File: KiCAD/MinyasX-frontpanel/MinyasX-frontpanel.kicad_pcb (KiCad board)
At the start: 2 copper layers, 96 x 21 mm, 30 parts, among them J101 Conn_01x04, J102 Conn_02x06_Odd_Even, SW101 SW_Push, SW102 SW_Push, U101 SLG46826G(V2), U102 JOYSTICK, U17 XC6201P332MR-G, U22 PCA9515DP

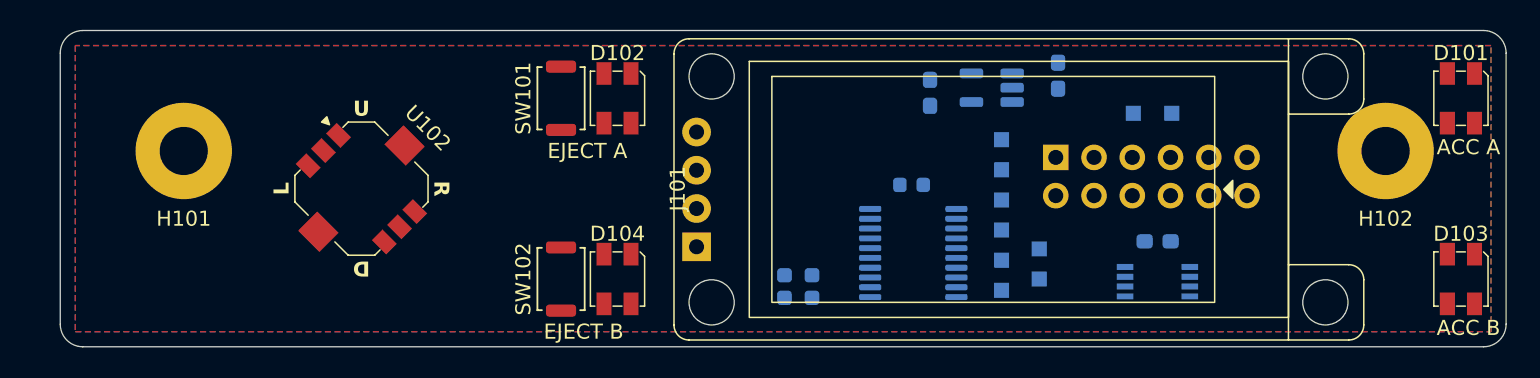
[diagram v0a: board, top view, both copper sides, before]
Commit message: * フロントパネルのキー操作ができるようにした * 画面のページ切り替えができるようにした * FDDの回転数とbpsの推定コードを修正した
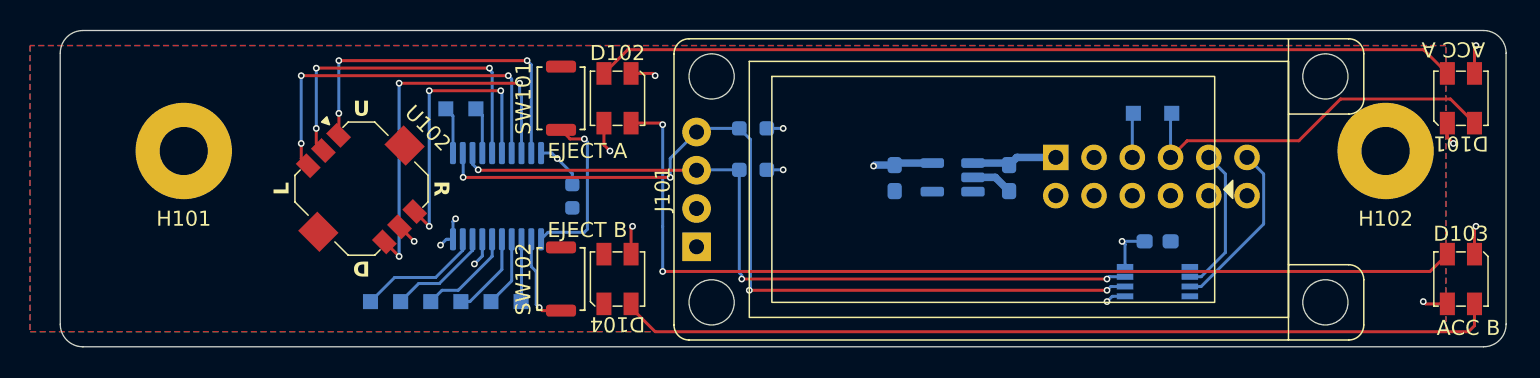
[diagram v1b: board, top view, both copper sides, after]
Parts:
- moved TP105 42.5 mm to (124.6, 95.0)
- moved TP106 42.0 mm to (122.6, 95.0)
- moved TP107 39.1 mm to (129.6, 82.2)
- moved TP108 38.8 mm to (127.6, 82.2)
- moved TP104 38.2 mm to (126.6, 95.0)
- moved TP103 36.5 mm to (128.6, 95.0)
- moved TP102 35.0 mm to (130.6, 95.0)
- moved TP101 33.7 mm to (132.6, 95.0)
- moved U101 27.9 mm to (131.0, 88.0), turned to 90 degrees
- moved C101 22.5 mm to (136.0, 88.0), turned to -90 degrees
- moved R31 11.6 mm to (148.0, 83.5), turned to 180 degrees
- moved R30 7.62 mm to (148.0, 86.2), turned to 180 degrees
- moved C25 7.54 mm to (165.0, 86.8)
- moved U17 6.49 mm to (161.2, 86.8)
- moved C26 6.13 mm to (157.4, 86.8)
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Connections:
- TP101 pad 1: Net-(U101-IO14) -> Net-(U101-IO12)
- TP102 pad 1: Net-(U101-IO13) -> Net-(U101-IO11)
- TP103 pad 1: Net-(U101-IO12) -> Net-(U101-IO10)
- TP104 pad 1: Net-(U101-IO11) -> Net-(U101-IO9)
- TP105 pad 1: Net-(U101-IO10) -> Net-(U101-IO8)
- TP106 pad 1: Net-(U101-IO9) -> Net-(U101-IO7)
- TP107 pad 1: Net-(U101-IO8) -> Net-(U101-IO5)
- TP108 pad 1: Net-(U101-IO7) -> Net-(U101-IO6)
- U101 pad 1: Net-(U101-IO14) -> /EJECT_A
- U101 pad 11: /EJECT_B -> Net-(U101-IO6)
- U101 pad 14: /EJECT_A -> Net-(U101-IO5)
- U101 pad 2: Net-(U101-IO13) -> /EJECT_B
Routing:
- net Net-(D102-DOUT): track 0.00 -> 64.5 mm, vias 0 -> 2
- net Net-(D103-DOUT): track 0.00 -> 58.5 mm
- net /I2C_SDA: track 0.00 -> 58.2 mm, vias 0 -> 4
- net Net-(D101-DOUT): track 0.00 -> 57.3 mm
- net /I2C_SCL: track 0.00 -> 51.5 mm, vias 0 -> 3
- net /DOWN: track 0.00 -> 25.6 mm, vias 0 -> 3
- net /LED_DATA: track 0.00 -> 25.4 mm
- net /LEFT: track 0.00 -> 25.2 mm, vias 0 -> 3
- net /UP: track 0.00 -> 23.7 mm, vias 0 -> 3
- net /CENTER: track 0.00 -> 23.0 mm, vias 0 -> 3
- net /RIGHT: track 0.00 -> 19.3 mm, vias 0 -> 3
- net +3.3V: track 0.00 -> 16.2 mm, vias 0 -> 7
- net VDD_MCU: track 0.00 -> 13.2 mm, vias 0 -> 4
- net GND: track 0.00 -> 11.7 mm, vias 0 -> 6
- net /I2C_SDA_5V: track 0.00 -> 11.5 mm
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- added copper zone on In1.Cu, net +3.3V
- added copper zone on In2.Cu, net VDD_MCU
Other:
- copper layers 2 -> 4

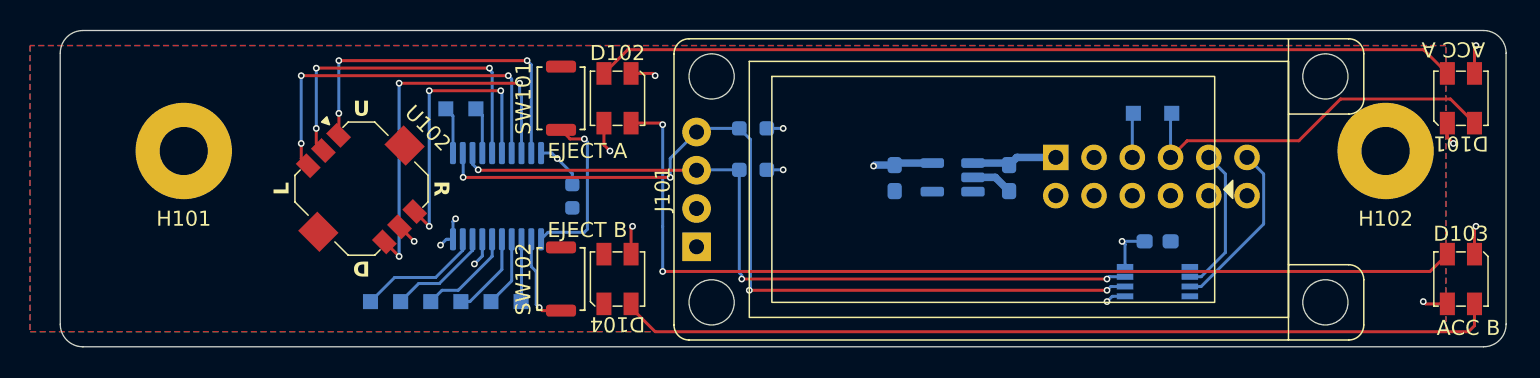
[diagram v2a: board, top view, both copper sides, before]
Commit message: フロントパネル周りの配線を見直した
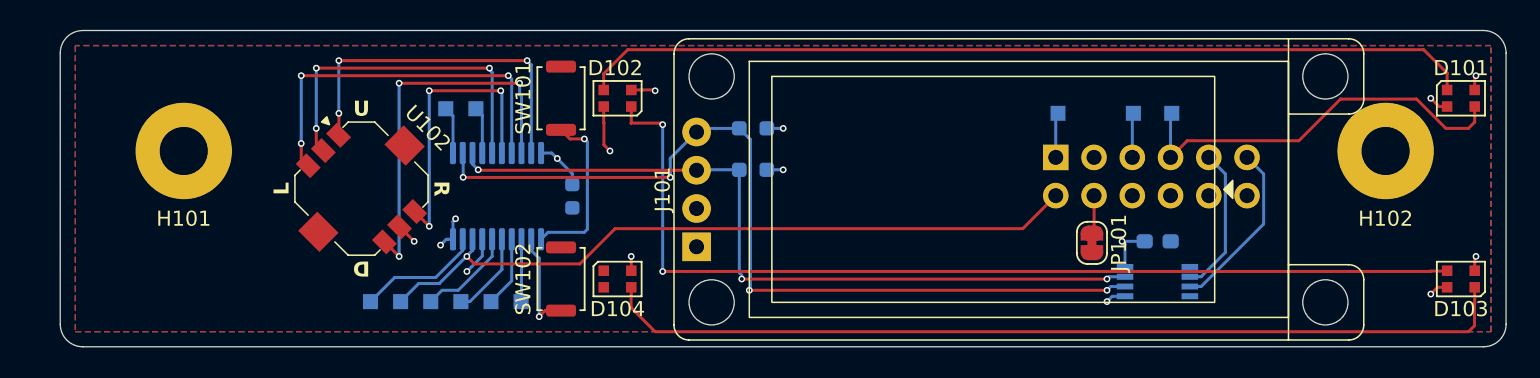
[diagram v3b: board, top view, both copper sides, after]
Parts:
- removed C25, C26: 1uF, Capacitor_SMD:C_0603_1608Metric_Pad1.08x0.95mm_HandSolder
- removed U17: XC6201P332MR-G, Package_TO_SOT_SMD:SOT-23-5_HandSoldering
- added JP101: Jumper_2_Bridged, Jumper:SolderJumper-2_P1.3mm_Bridged_RoundedPad1.0x1.5mm, F.Cu at (170.5, 91.1)
- added TP110: TestPoint, TestPoint:TestPoint_Pad_1.0x1.0mm, B.Cu at (173.2, 82.5)
- D101, D102, D103, D104: value SK6812MINI -> WS2812B-2020; footprint x68k-lib:SK6812MINI-HS -> LED_SMD:LED_WS2812B-2020_PLCC4_2.0x2.0mm
- moved TP109 5.00 mm to (168.2, 82.5)
- turned D101 to 0 degrees
- turned D102 to 180 degrees
- turned D103 to 180 degrees
- turned D104 to 0 degrees
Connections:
- D101 pad 1: GND -> Net-(D101-DOUT)
- D101 pad 2: /LED_DATA -> GND
- D101 pad 3: VDD_MCU -> /LED_DATA
- D101 pad 4: Net-(D101-DOUT) -> VDD_MCU
- D102 pad 1: GND -> Net-(D102-DOUT)
- D102 pad 2: Net-(D101-DOUT) -> GND
- D102 pad 3: VDD_MCU -> Net-(D101-DOUT)
- D102 pad 4: Net-(D102-DOUT) -> VDD_MCU
- D103 pad 1: GND -> Net-(D103-DOUT)
- D103 pad 2: Net-(D102-DOUT) -> GND
- D103 pad 3: VDD_MCU -> Net-(D102-DOUT)
- D103 pad 4: Net-(D103-DOUT) -> VDD_MCU
- D104 pad 1: GND -> unconnected-(D104-DOUT-Pad1)
- D104 pad 2: Net-(D103-DOUT) -> GND
- D104 pad 3: VDD_MCU -> Net-(D103-DOUT)
- D104 pad 4: unconnected-(D104-DOUT-Pad4) -> VDD_MCU
- J102 pad 2: GND -> /CONT_PUSH
- J102 pad 4: GND -> Net-(J102-Pin_4)
- J102 pad 5: /CONTROLLER_OPTION -> +3.3V
- TP105 pad 1: Net-(U101-IO8) -> /CONT_PUSH
- TP109 pad 1: /CONTROLLER_OPTION -> VDD_MCU
- U101 pad 8: Net-(U101-IO8) -> /CONT_PUSH
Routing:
- net /CONT_PUSH: track 0.00 -> 48.1 mm, vias 0 -> 1
- net Net-(U101-IO8): track 6.92 -> 0.00 mm
- net GND: track 11.7 -> 7.70 mm
- net VDD_MCU: track 13.2 -> 9.32 mm
- net /CONTROLLER_OPTION: track 2.95 -> 0.00 mm
- net Net-(J102-Pin_4): track 0.00 -> 2.54 mm
- net Net-(D103-DOUT): track 58.5 -> 60.7 mm
- net Net-(D101-DOUT): track 57.3 -> 59.5 mm
- net /LED_DATA: track 25.4 -> 26.8 mm
- net /EJECT_B: track 6.29 -> 6.97 mm
- net Net-(D102-DOUT): track 64.5 -> 65.1 mm
- net +3.3V: track 16.2 -> 15.7 mm, vias 7 -> 6
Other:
- board text added: "3.3"
- board text added: "LED"
- board text added: "VDD"

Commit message: v2.1.0のPCBA発注
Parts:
- renumbered C101 to C2001, C37 to C2002, D101 to D2001, D102 to D2002, D103 to D2003, D104 to D2004, H101 to H2001, H102 to H2002, J102 to J2001, J101 to J2002, JP101 to JP2001, R30 to R2001, R31 to R2002, SW101 to SW2001, SW102 to SW2002, TP109 to TP2001, TP110 to TP2002, TP112 to TP2003, TP101 to TP2004, TP102 to TP2005, TP103 to TP2006, TP104 to TP2007, TP105 to TP2008, TP106 to TP2009, TP107 to TP2010, TP108 to TP2011, U101 to U2001, U22 to U2002, U102 to U2003

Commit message: 細かい基板のパッチを当てた * MODE_SELECT をGPからドライブできるように配線した * FDD電源出力コネクタを少し外に出した * GP1、GP5のI2Cを切り離せるようにした * GP5のI2C を5V系に変更 * WCH-LinkE の接続コネクタが鏡像になっていた問題を修正
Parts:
- added JP2002: Jumper_2_Small_Open, Jumper:SolderJumper-2_P1.3mm_Open_RoundedPad1.0x1.5mm, B.Cu at (135.5, 79.5)
- moved C2002 22.5 mm to (155.0, 80.5)
- moved U2002 22.5 mm to (155.0, 83.2)
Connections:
- U2001 pad 12: /I2C_SDA -> Net-(JP2002-A)
- U2001 pad 13: /I2C_SCL -> /I2C_SCL_5V
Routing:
- net /I2C_SDA: track 58.2 -> 9.29 mm, vias 4 -> 0
- net /I2C_SCL_5V: track 9.80 -> 56.9 mm, vias 0 -> 2
- net /I2C_SDA_5V: track 11.5 -> 52.6 mm
- net /I2C_SCL: track 51.5 -> 12.9 mm, vias 3 -> 1
- net Net-(JP2002-A): track 0.00 -> 12.7 mm
- net /LED_DATA: track 26.8 -> 27.7 mm
- net GND: vias 6 -> 23
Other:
- board text added: "GP5"
- board text added: "Minyas X Frontpanel ${REVISION}"
